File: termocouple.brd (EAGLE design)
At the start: 69.8 x 100 mm, 20 parts, among them IC1 MAX6675, IC2 MAX6675, IC3 MAX6675, IC4 MAX6675, U2 TC1262_VDB, X2 1751248, X3 1751248, X4 1751248, X5 1751248

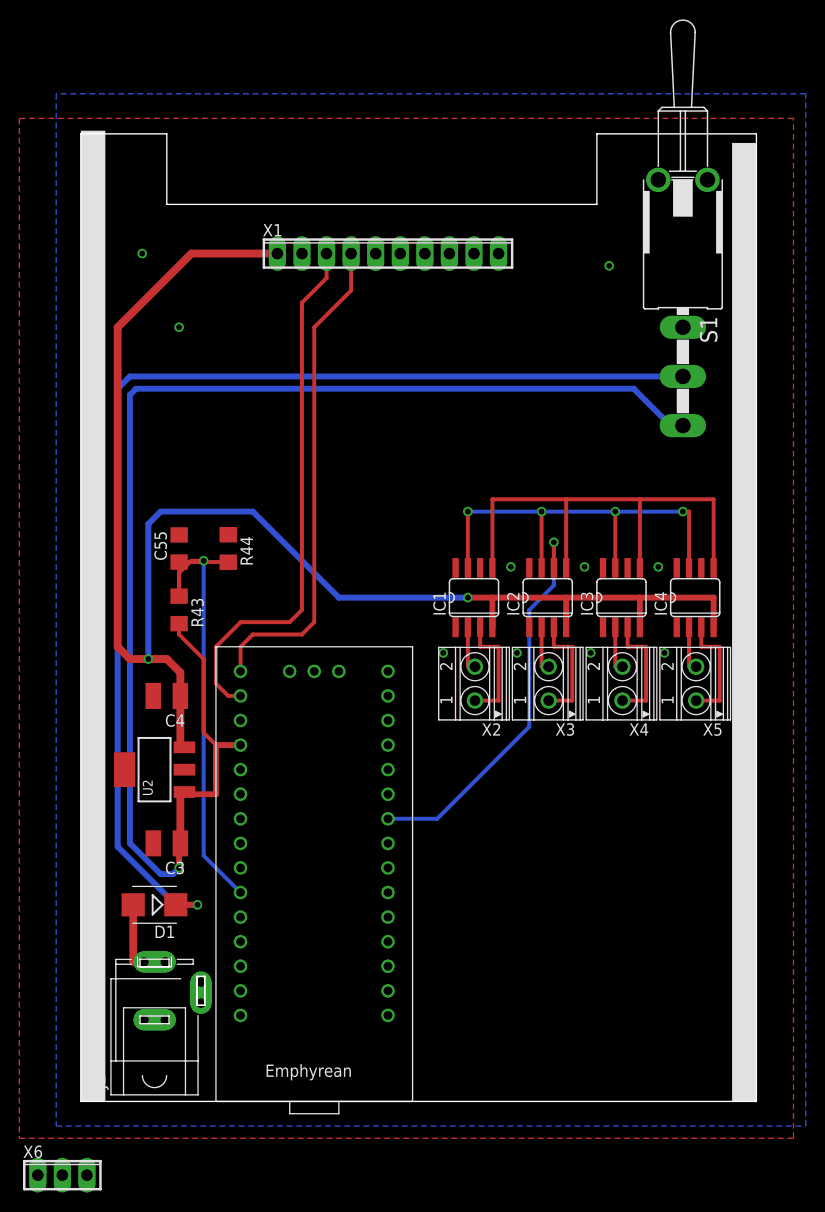
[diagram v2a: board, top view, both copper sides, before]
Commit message: BRD added thermocouple device
thermocouple
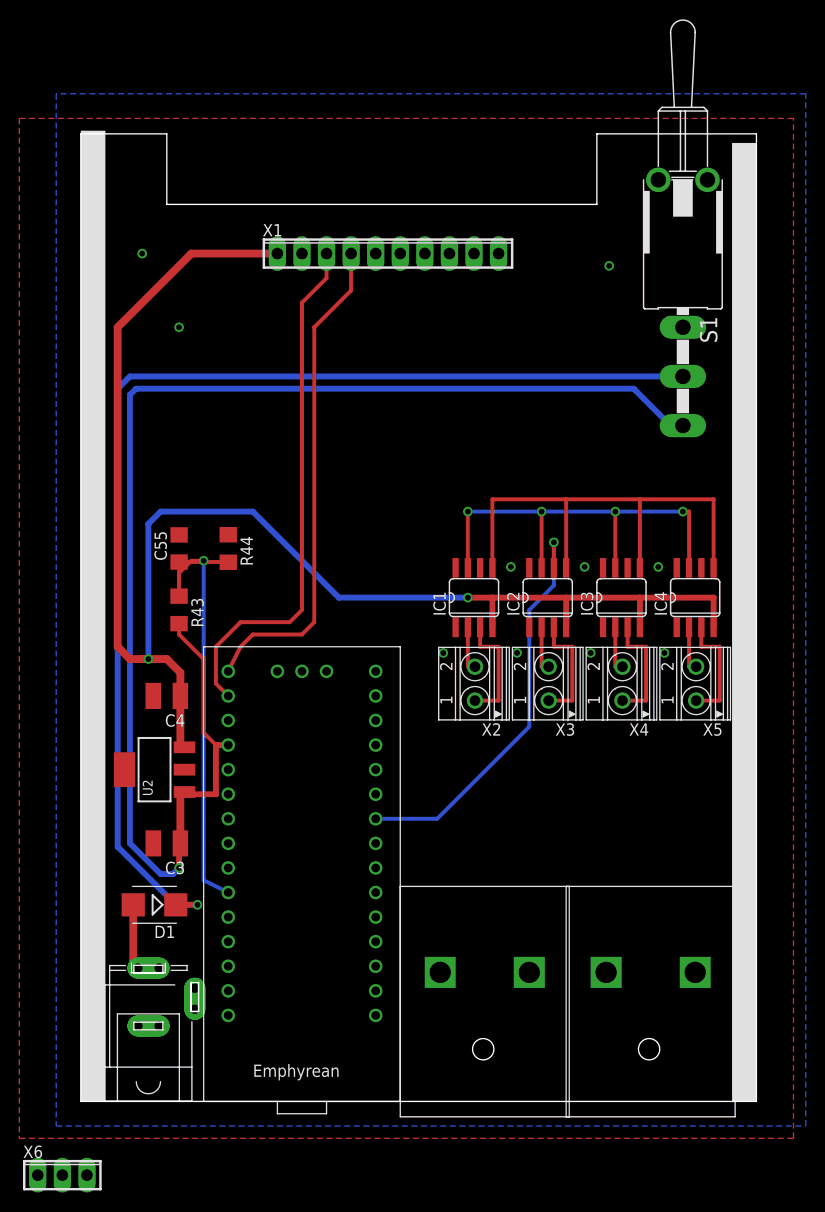
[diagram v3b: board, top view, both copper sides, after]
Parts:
- added U$2, U$3: THERMOCOUPLE, mine:THERMOCOUPLE
- moved U$1 1.27 mm to (22.9, 26.7)
- moved J2 0.90 mm to (6.99, 10.8)
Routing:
- net N$5: track 55.2 -> 54.0 mm
- net N$3: track 41.3 -> 42.6 mm
- net +12V: track 146.2 -> 144.9 mm
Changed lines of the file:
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@@
 </autorouter>
 <elements>
-<element name="U$1" library="mine" package="EMPHYREAN" value="EPHYREAN" x="24.13" y="26.67"/>
+<element name="U$1" library="mine" package="EMPHYREAN" value="EPHYREAN" x="22.86" y="26.67"/>
 <element name="IC1" library="adafruit" package="SO08" value="MAX6675" x="40.64" y="52.07"/>
 <element name="IC2" library="adafruit" package="SO08" value="MAX6675" x="48.26" y="52.07"/>
@@
 <element name="C3" library="rcl" package="C1210" value="10u (1210)" x="8.89" y="26.67" rot="R180"/>
 <element name="C4" library="rcl" package="C1210" value="10u (1210)" x="8.89" y="41.91" rot="R180"/>
-<element name="J2" library="PI Teensy" package="SPC4078" value="" x="7.62" y="11.43" rot="R90"/>
+<element name="J2" library="PI Teensy" package="SPC4078" value="" x="6.985" y="10.795" rot="R90"/>
 <element name="S1" library="switch" package="LPV-1" value="" x="62.23" y="95.25" rot="R180"/>
 <element name="D1" library="diode" package="SMB" value="VS-10BQ015-M3" x="7.62" y="20.32" rot="R180"/>
@@
 <attribute name="OC_FARNELL" value="unknown" x="-1.905" y="-7.62" size="1.778" layer="27" display="off"/>
 </element>
+<element name="U$2" library="mine" package="THERMOCOUPLE" value="THERMOCOUPLE" x="57.785" y="10.795"/>
+<element name="U$3" library="mine" package="THERMOCOUPLE" value="THERMOCOUPLE" x="40.64" y="10.795"/>
 </elements>
 <signals>
@@
 <wire x1="40.005" y1="60.96" x2="47.625" y2="60.96" width="0.4064" layer="16"/>
 <contactref element="U$1" pad="D7"/>
-<wire x1="31.75" y1="21.59" x2="40.005" y2="55.1434" width="0" layer="19" extent="1-1"/>
+<wire x1="30.48" y1="21.59" x2="40.005" y2="55.1434" width="0" layer="19" extent="1-1"/>
 </signal>
 <signal name="N$2">
@@
 <wire x1="42.545" y1="55.1434" x2="42.545" y2="62.23" width="0.4064" layer="1"/>
 <contactref element="U$1" pad="D8"/>
-<wire x1="31.75" y1="24.13" x2="42.545" y2="55.1434" width="0" layer="19" extent="1-1"/>
+<wire x1="30.48" y1="24.13" x2="42.545" y2="55.1434" width="0" layer="19" extent="1-1"/>
 </signal>
 <signal name="+3V3">
@@
 <via x="37.465" y="46.355" extent="1-16" drill="0.6" shape="square"/>
 <contactref element="X6" pad="1"/>
-<wire x1="6.53435" y1="8.443909375" x2="-4.445" y2="-7.62" width="0" layer="19" extent="1-1"/>
+<wire x1="5.89935" y1="7.808909375" x2="-4.445" y2="-7.62" width="0" layer="19" extent="1-1"/>
 </signal>
 <signal name="N$4">
 <contactref element="IC1" pad="6"/>
 <contactref element="U$1" pad="D9"/>
-<wire x1="31.75" y1="26.67" x2="41.275" y2="55.1434" width="0" layer="19" extent="1-1"/>
+<wire x1="30.48" y1="26.67" x2="41.275" y2="55.1434" width="0" layer="19" extent="1-1"/>
 </signal>
 <signal name="N$6">
 <contactref element="IC3" pad="6"/>
 <contactref element="U$1" pad="D11"/>
-<wire x1="31.75" y1="31.75" x2="56.515" y2="55.1434" width="0" layer="19" extent="1-1"/>
+<wire x1="30.48" y1="31.75" x2="56.515" y2="55.1434" width="0" layer="19" extent="1-1"/>
 </signal>
 <signal name="N$7">
 <contactref element="IC4" pad="6"/>
 <contactref element="U$1" pad="D12"/>
-<wire x1="31.75" y1="34.29" x2="64.135" y2="55.1434" width="0" layer="19" extent="1-1"/>
+<wire x1="30.48" y1="34.29" x2="64.135" y2="55.1434" width="0" layer="19" extent="1-1"/>
 </signal>
 <signal name="+12V">
@@
 <wire x1="10.29" y1="31.9786" x2="10.29" y2="27.305" width="0.8128" layer="1"/>
 <wire x1="10.29" y1="27.305" x2="10.29" y2="26.67" width="0.8128" layer="1"/>
-<wire x1="16.51" y1="36.83" x2="13.97" y2="36.83" width="0.6096" layer="1"/>
+<wire x1="15.24" y1="36.83" x2="13.97" y2="36.83" width="0.6096" layer="1"/>
 <wire x1="13.97" y1="36.83" x2="13.97" y2="31.75" width="0.6096" layer="1"/>
 <wire x1="13.97" y1="31.75" x2="10.7188" y2="31.75" width="0.6096" layer="1"/>
@@
 <wire x1="11.43" y1="55.88" x2="12.7" y2="55.88" width="0.4064" layer="1"/>
 <via x="12.7" y="55.88" extent="1-16" drill="0.6" shape="square"/>
-<wire x1="12.7" y1="55.88" x2="12.7" y2="25.4" width="0.4064" layer="16"/>
-<wire x1="12.7" y1="25.4" x2="16.51" y2="21.59" width="0.4064" layer="16"/>
+<wire x1="12.7" y1="55.88" x2="12.7" y2="22.86" width="0.4064" layer="16"/>
+<wire x1="12.7" y1="22.86" x2="15.24" y2="21.59" width="0.4064" layer="16"/>
 </signal>
 <signal name="N$5">
 <contactref element="U$1" pad="SDA"/>
 <contactref element="X1" pad="3"/>
-<wire x1="16.51" y1="41.91" x2="15.24" y2="41.91" width="0.4064" layer="1"/>
 <wire x1="15.24" y1="41.91" x2="13.97" y2="43.18" width="0.4064" layer="1"/>
 <wire x1="13.97" y1="43.18" x2="13.97" y2="46.99" width="0.4064" layer="1"/>
@@
 <wire x1="22.86" y1="48.26" x2="17.78" y2="48.26" width="0.4064" layer="1"/>
 <wire x1="17.78" y1="48.26" x2="16.51" y2="46.99" width="0.4064" layer="1"/>
-<wire x1="16.51" y1="46.99" x2="16.51" y2="44.45" width="0.4064" layer="1"/>
+<wire x1="16.51" y1="46.99" x2="15.24" y2="44.45" width="0.4064" layer="1"/>
 </signal>
 <signal name="N$13">
@@
 <contactref element="J2" pad="6"/>
 <contactref element="D1" pad="A"/>
-<wire x1="6.52789375" y1="14.41279375" x2="5.42" y2="14.41279375" width="0.8128" layer="1"/>
+<wire x1="5.89289375" y1="13.77779375" x2="5.42" y2="14.41279375" width="0.8128" layer="1"/>
 <wire x1="5.42" y1="14.41279375" x2="5.42" y2="20.32" width="0.8128" layer="1"/>
-<wire x1="6.52789375" y1="14.41279375" x2="8.73125" y2="14.43" width="0" layer="19" extent="1-1"/>
+<wire x1="5.89289375" y1="13.77779375" x2="8.09625" y2="13.795" width="0" layer="19" extent="1-1"/>
 </signal>
 <signal name="N$14">
@@
 <contactref element="U$1" pad="D10"/>
 <contactref element="IC2" pad="6"/>
-<wire x1="31.75" y1="29.21" x2="36.83" y2="29.21" width="0.4064" layer="16"/>
+<wire x1="30.48" y1="29.21" x2="36.83" y2="29.21" width="0.4064" layer="16"/>
 <wire x1="36.83" y1="29.21" x2="46.355" y2="38.735" width="0.4064" layer="16"/>
 <wire x1="46.355" y1="38.735" x2="46.355" y2="50.8" width="0.4064" layer="16"/>
@@
 <contactref element="U$1" pad="D6"/>
 <contactref element="X1" pad="5"/>
-<wire x1="31.75" y1="19.05" x2="30.48" y2="87.63" width="0" layer="19" extent="1-1"/>
+<wire x1="30.48" y1="19.05" x2="30.48" y2="87.63" width="0" layer="19" extent="1-1"/>
 </signal>
 <signal name="N$10">
@@
 <contactref element="U$1" pad="D4"/>
 <contactref element="X1" pad="7"/>
-<wire x1="31.75" y1="13.97" x2="35.56" y2="87.63" width="0" layer="19" extent="1-1"/>
+<wire x1="30.48" y1="13.97" x2="35.56" y2="87.63" width="0" layer="19" extent="1-1"/>
 </signal>
 <signal name="N$12">
 <contactref element="U$1" pad="D3"/>
 <contactref element="X1" pad="8"/>
-<wire x1="31.75" y1="11.43" x2="38.1" y2="87.63" width="0" layer="19" extent="1-1"/>
+<wire x1="30.48" y1="11.43" x2="38.1" y2="87.63" width="0" layer="19" extent="1-1"/>
 </signal>
 <signal name="N$22">
 <contactref element="U$1" pad="D0"/>
 <contactref element="X6" pad="3"/>
-<wire x1="0.635" y1="-7.62" x2="16.51" y2="11.43" width="0" layer="19" extent="1-1"/>
+<wire x1="0.635" y1="-7.62" x2="15.24" y2="11.43" width="0" layer="19" extent="1-1"/>
 </signal>
 <signal name="N$23">
 <contactref element="U$1" pad="D1"/>
 <contactref element="X6" pad="2"/>
-<wire x1="-1.905" y1="-7.62" x2="16.51" y2="8.89" width="0" layer="19" extent="1-1"/>
+<wire x1="-1.905" y1="-7.62" x2="15.24" y2="8.89" width="0" layer="19" extent="1-1"/>
 </signal>
 </signals>

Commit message: readme update, arm definitions, pcb moved to 2 sensor
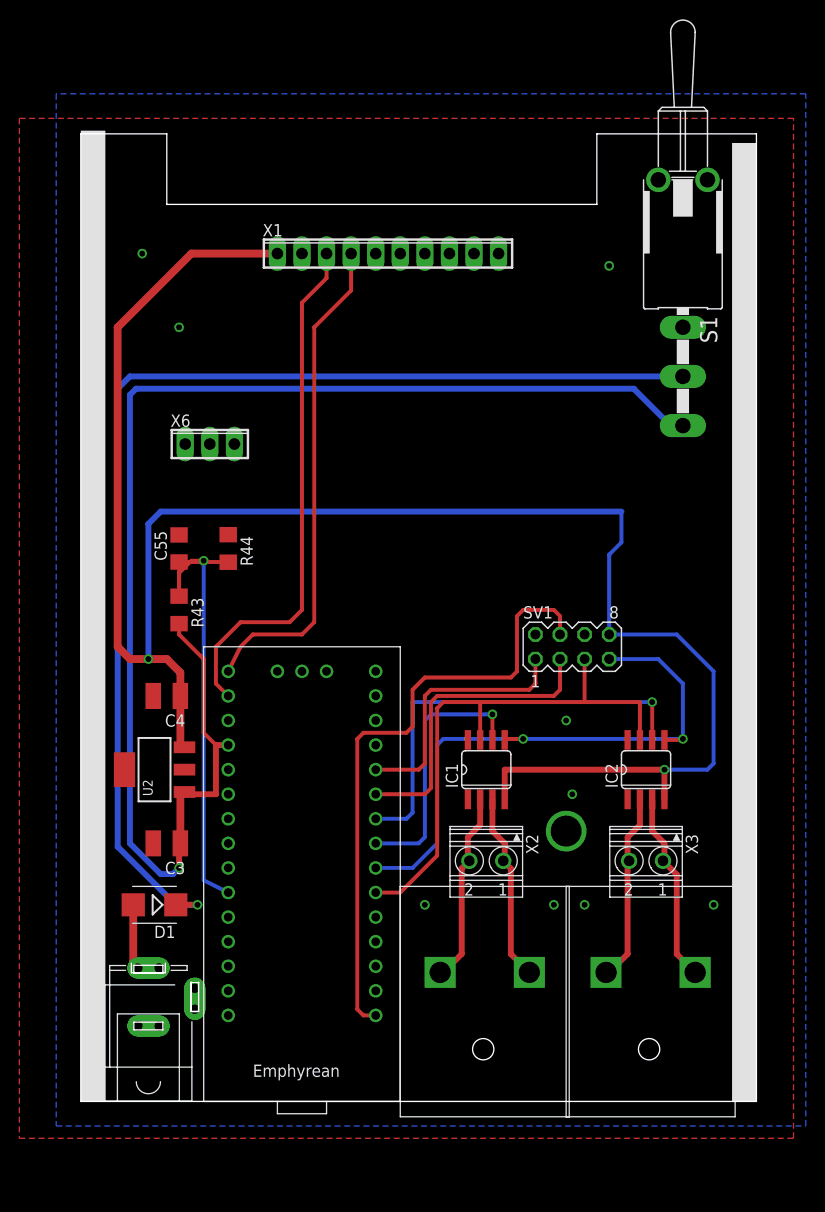
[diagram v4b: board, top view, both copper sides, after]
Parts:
- removed IC3, IC4: MAX6675, adafruit:SO08
- removed X4, X5: 1751248, con-phoenix-350:1751248
- added SV1: (no value), con-lstb:MA04-2
- moved X6 77.1 mm to (13.3, 67.9)
- moved X3 21.0 mm to (58.4, 24.8), turned to 180 degrees
- moved IC2 20.5 mm to (58.4, 34.3)
- moved X2 18.5 mm to (41.9, 24.8), turned to 180 degrees
- moved IC1 17.8 mm to (41.9, 34.3)
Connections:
- removed net N$16: IC3.2, X4.2
- removed net N$17: IC3.3, X4.1
- removed net N$6: IC3.6, U$1.D11
- net +3V3: now also SV1.8; no longer IC3.4, IC4.4
- net GND: now also SV1.2, SV1.6; no longer IC3.1, IC4.1
- net N$1: now also SV1.5; no longer IC3.7, IC4.7
- net N$14: now also SV1.1, U$1.D12; no longer IC4.3, X5.1
- net N$15: now also SV1.4, U$1.D2; no longer IC4.2, X5.2
- net N$18: now also U$2.POS
- net N$19: now also U$2.NEG
- net N$2: now also SV1.7; no longer IC3.5, IC4.5
- net N$20: now also U$3.POS
- net N$21: now also U$3.NEG
- net N$7: now also SV1.3, U$1.D11; no longer IC4.6, U$1.D12
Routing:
- net N$15: track 4.80 -> 64.3 mm
- net +3V3: track 157.3 -> 194.9 mm
- net N$7: track 0.00 -> 31.9 mm
- net N$4: track 0.00 -> 27.3 mm, vias 0 -> 1
- net N$21: track 4.80 -> 19.9 mm
- net N$14: track 11.9 -> 26.8 mm
- net N$19: track 4.80 -> 19.6 mm
- net N$17: track 11.9 -> 0.00 mm
- net N$1: track 46.1 -> 56.7 mm, vias 4 -> 0
- net N$2: track 51.2 -> 61.5 mm, vias 0 -> 2
- net N$18: track 11.9 -> 19.9 mm
- net N$20: track 11.9 -> 19.6 mm
- net N$16: track 4.80 -> 0.00 mm
- net N$3: track 42.6 -> 44.2 mm
